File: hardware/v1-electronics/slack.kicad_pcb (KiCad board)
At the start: 2 copper layers, 399.2 x 265.1 mm, 408 parts, among them IC1 TPS61288LRQQR, IC2 MP2721GRH-0000-Z, IC3 IS31FL3733-QFLS4-TR, IC4 IS31FL3733-QFLS4-TR, J1 Female USB-C USB2.0, J2 XT30PW-M, J3 Female JST-SH, Q1 AON7423, SW1 MSwitch, SW10 MSwitch, SW11 MSwitch, SW12 MSwitch, SW13 MSwitch, SW14 MSwitch, SW15 MSwitch, SW16 MSwitch, SW17 MSwitch, SW18 MSwitch, SW19 MSwitch, SW2 MSwitch, SW20 MSwitch, SW23 MSwitch, SW24 MSwitch, SW25 MSwitch, SW26 MSwitch, SW27 MSwitch, SW28 MSwitch, SW29 MSwitch, SW3 MSwitch, SW30 MSwitch, SW31 MSwitch, SW32 MSwitch, SW33 MSwitch, SW34 MSwitch, SW37 MSwitch, SW38 MSwitch, SW39 MSwitch, SW4 MSwitch, SW40 MSwitch, SW41 MSwitch, SW42 MSwitch, SW43 MSwitch, SW44 MSwitch, SW45 MSwitch, SW46 MSwitch, SW47 MSwitch, SW48 MSwitch, SW5 MSwitch, SW51 MSwitch, SW52 MSwitch, SW53 MSwitch, SW54 MSwitch, SW55 MSwitch, SW56 MSwitch, SW57 MSwitch, SW58 MSwitch, SW59 MSwitch, SW6 MSwitch, SW60 MSwitch, SW61 MSwitch, SW62 SW_Push, SW63 SW_Push, SW64 MSwitch, SW65 MSwitch, SW66 MSwitch, SW67 MSwitch, SW68 MSwitch, SW69 SSSS820201, SW7 2TED3M6RES, SW70 SSSS820201, SW71 SSSS820201, SW72 SSSS820201, SW73 SSSS820201, SW74 SPEF110100, SW75 SPEF110100, SW76 SPEF110100, SW77 SPEF110100, SW78 SSSS820201, SW79 SSSS820201, SW8 SW_Push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

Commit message: feat(v1 hardware): update LED,Track Point, and Switch footprints
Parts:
- REF** (x2): value TP_Sprintek_SK8707-01_Sensor_reversible -> TP_Sprintek_SK8707-01-004; footprint Amazon:TP_Sprintek_SK8707-01_Sensor_reversible -> Amazon:TP_Sprintek_SK8707-01-004
- moved LED527 472.1 mm to (0.00, 0.00)
- moved LED526 470.1 mm to (0.00, 0.00)
- moved LED525 468.1 mm to (0.00, 0.00)
- moved LED524 466.1 mm to (0.00, 0.00)
- moved LED523 464.2 mm to (0.00, 0.00)
- moved LED522 462.4 mm to (0.00, 0.00)
- moved LED521 460.5 mm to (0.00, 0.00)
- moved C26 459.5 mm to (0.00, 0.00)
- moved C32 459.4 mm to (0.00, 0.00)
- moved R45 459.2 mm to (0.00, 0.00)
- moved C30 458.5 mm to (0.00, 0.00)
- moved C28 457.6 mm to (0.00, 0.00)
- moved R47 456.4 mm to (0.00, 0.00)
- moved R46 455.0 mm to (0.00, 0.00)
- moved IC4 454.1 mm to (0.00, 0.00)
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
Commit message: feat(v1 hardware): mid component update save
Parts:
- added REF**: grounded_scrollcap, Mechanical:grounded_scrollcap, F.Cu at (141.4, 210.7)
- added REF**: switched_grounded_scrollcap, Mechanical:switched_grounded_scrollcap, F.Cu at (303.0, 211.2)
- SW62: footprint XKB Connection:TC-1109-C-E -> ALPS Electric:SKQGAKE010
- SW8: footprint Button_Switch_SMD:SW_Push_1P1T_XKB_TS-1187A -> ALPS Electric:SKQGAKE010
- moved LED527 472.1 mm to (416.6, 222.0)
- moved LED526 470.1 mm to (416.6, 217.7)
- moved LED525 468.1 mm to (416.6, 213.4)
- moved LED524 466.1 mm to (416.6, 209.1)
- moved LED523 464.2 mm to (416.6, 204.8)
- moved LED522 462.4 mm to (416.6, 200.5)
- moved LED521 460.5 mm to (416.6, 196.2)
- moved C26 459.5 mm to (406.0, 215.1)
- moved C32 459.4 mm to (408.5, 210.2)
- moved R45 459.2 mm to (404.4, 217.6)
- moved C30 458.5 mm to (408.5, 208.2)
- moved C28 457.6 mm to (408.5, 206.2)
- moved R47 456.4 mm to (401.0, 218.0)
- moved R46 455.0 mm to (401.0, 215.0)
- moved IC4 454.1 mm to (402.9, 209.4)
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
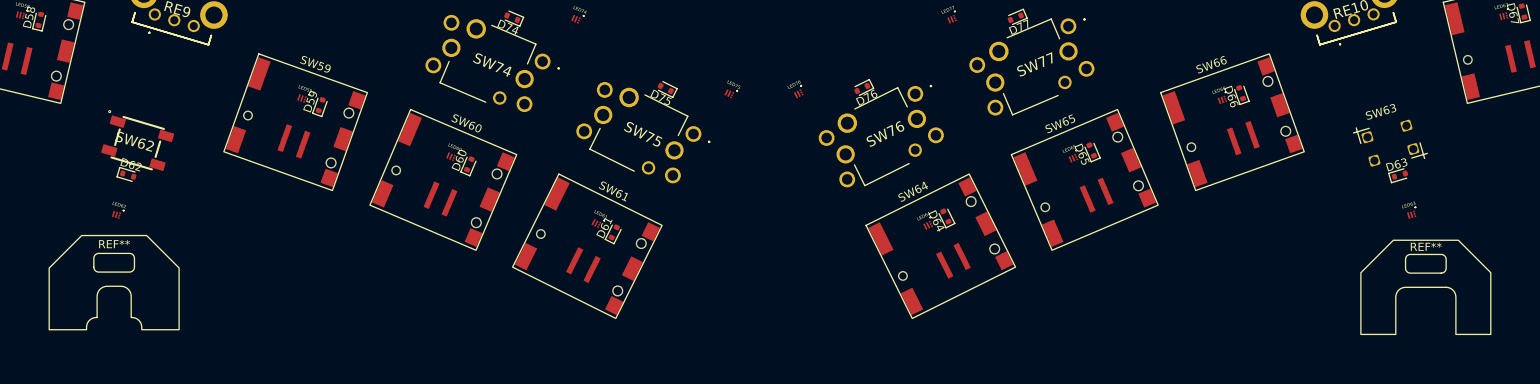
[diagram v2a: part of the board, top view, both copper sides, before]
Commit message: feat(v1 hardware): update components
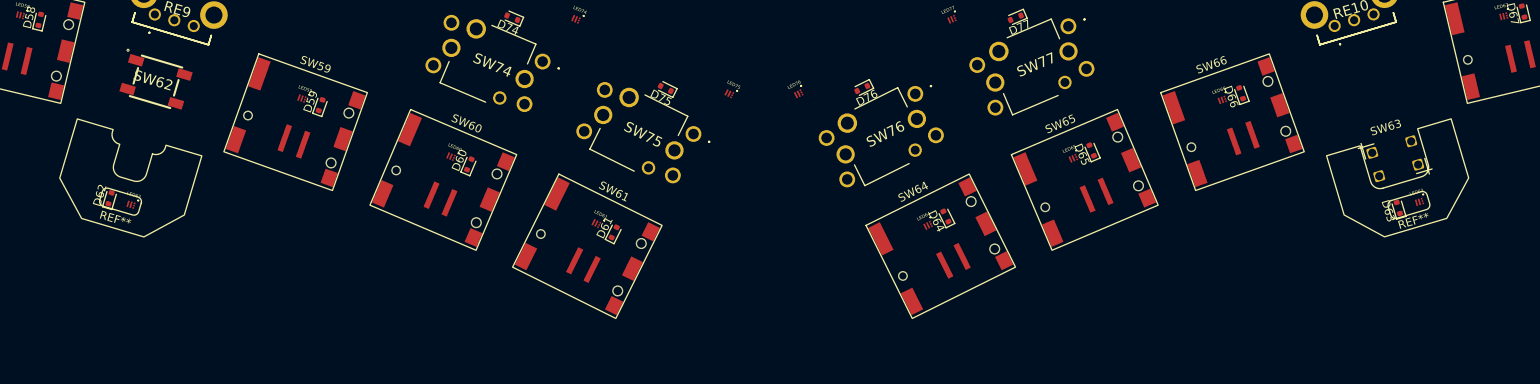
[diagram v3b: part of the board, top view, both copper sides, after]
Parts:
- moved REF** 24.7 mm to (298.4, 187.0), turned to -163.48 degrees
- moved REF** 23.9 mm to (144.5, 187.0), turned to 163.481 degrees
- moved SW62 7.89 mm to (146.6, 180.1)
- moved D63 4.05 mm to (299.6, 195.7), turned to 106.52 degrees
- moved D62 3.63 mm to (140.9, 194.5), turned to 73.481 degrees
- moved LED62 2.18 mm to (143.5, 195.3), turned to -16.519 degrees
- moved SW63 2.00 mm to (299.2, 189.6)
- moved LED63 1.85 mm to (302.2, 194.9)
